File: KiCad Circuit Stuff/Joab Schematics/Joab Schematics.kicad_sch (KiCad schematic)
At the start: 0 parts

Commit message: Added some things
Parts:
- added J1: Conn_02x16_Odd_Even, symbol Connector_Generic:Conn_02x16_Odd_Even
- added U1: TPS613222ADBV, Package_TO_SOT_SMD:SOT-23-5, symbol Regulator_Switching:TPS613222ADBV
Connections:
- new net Battery: J1.14 (Pin_14), U1.1 (SW)
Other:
- note added: "INA219 Battery Chargin mode Charge with USBC 3v3 and 5v regulation (bost to 5, linear down to 3.3)"
- note added: "JOAB YOUR SHIT HERE"
- note added: "PIN Layout 1: Motor2_B_Out 2: Motor2_A_Out 3: Mitir4_A_Out 4: Motor 5: Motor 6: Motor 7: CTRL_Ext_Load2 8: Motor 9: USART2_RX 10: Motor 11: EXT_Load2_Out 12: Usart2_TX 13: Fast_Charge_Ctrl 14: battery 15: rsv 16: i2C1_SCL 17: i2C1_SDA 18: 3v3 out 19: gnd 20: 5v out 21: ext_load1_out 22: HV 23: Gnd 24: motor 25: ctrl ext load1 26: motor 27: motor 28: motor 29: motor 30: motor 31: motor 32: motor"
- company: (none) -> UCT
- title: (none) -> Joab PCP Work
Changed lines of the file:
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@@
 (kicad_sch (version 20230121) (generator eeschema)
   (paper "A4")
-  (label "JOAB YOUR SHIT HERE" (at 132.08 102.87 0) (fields_autoplaced)
+  (title_block
+    (title "Joab PCP Work")
+    (date "2025-03-19")
+    (rev "V0.0")
+    (company "UCT")
+    (comment 4 "KLPJOA002")
+  )
+  (wire (pts (xy 146.05 107.95) (xy 146.05 142.24))
+    (stroke (width 0) (type default))
+  )
+  (wire (pts (xy 146.05 107.95) (xy 168.91 107.95))
+    (stroke (width 0) (type default))
+  )
+  (polyline (pts (xy 68.58 12.7) (xy 68.58 59.69))
+    (stroke (width 0) (type default))
+  )
+  (polyline (pts (xy 12.7 59.69) (xy 68.58 59.69))
+    (stroke (width 0) (type default))
+  )
+  (text "INA219\nBattery Chargin mode\nCharge with USBC\n3v3 and 5v regulation (bost to 5, linear down to 3.3)\n\n"
+    (at 12.7 33.02 0)
     (effects (font (size 1.27 1.27)) (justify left bottom))
   )
+  (text "PIN Layout\n1: Motor2_B_Out\n2: Motor2_A_Out\n3: Mitir4_A_Out\n4: Motor\n5: Motor\n6: Motor\n7: CTRL_Ext_Load2\n8: Motor\n9: USART2_RX\n10: Motor\n11: EXT_Load2_Out\n12: Usart2_TX\n13: Fast_Charge_Ctrl\n14: battery\n15: rsv\n16: i2C1_SCL\n17: i2C1_SDA\n18: 3v3 out\n19: gnd\n20: 5v out\n21: ext_load1_out\n22: HV\n23:	Gnd\n24: motor\n25: ctrl ext load1\n26: motor\n27: motor\n28: motor\n29: motor\n30: motor\n31: motor\n32: motor"
+    (at 76.2 191.77 0)
+    (effects (font (size 1.27 1.27)) (justify left bottom))
+  )
+  (text "JOAB YOUR SHIT HERE" (at 26.67 15.24 0)
+    (effects (font (size 1.27 1.27)) (justify left bottom))
+  )
+  (label "Battery" (at 146.05 137.16 0) (fields_autoplaced)
+    (effects (font (size 1.27 1.27)) (justify left bottom))
+  )
+  (symbol (lib_id "Regulator_Switching:TPS613222ADBV") (at 179.07 110.49 0) (unit 1)
+    (in_bom yes) (on_board yes) (dnp no) (fields_autoplaced)
+    (property "Reference" "U1" (at 179.07 101.6 0)
+      (effects (font (size 1.27 1.27)))
+    )
+    (property "Value" "TPS613222ADBV" (at 179.07 104.14 0)
+      (effects (font (size 1.27 1.27)))
+    )
+    (property "Footprint" "Package_TO_SOT_SMD:SOT-23-5" (at 179.07 130.81 0)
+      (effects (font (size 1.27 1.27)) hide)
+    )
+    (property "Datasheet" "http://www.ti.com/lit/ds/symlink/tps61322.pdf" (at 179.07 114.3 0)
+      (effects (font (size 1.27 1.27)) hide)
+    )
+    (pin "1")
+    (pin "2")
+    (pin "3")
+    (pin "4")
+    (pin "5")
+    (instances
+      (project "Joab Schematics"
+        (path "/40536255-d30b-4646-9a8a-71849f0da59a"
+          (reference "U1") (unit 1)
+        )
+      )
+    )
+  )
+  (symbol (lib_id "Connector_Generic:Conn_02x16_Odd_Even") (at 143.51 149.86 270) (mirror x) (unit 1)
+    (in_bom yes) (on_board yes) (dnp no) (fields_autoplaced)
+    (property "Reference" "J1" (at 120.65 147.955 90)
+      (effects (font (size 1.27 1.27)) (justify right))
+    )
+    (property "Value" "Conn_02x16_Odd_Even" (at 120.65 150.495 90)
+      (effects (font (size 1.27 1.27)) (justify right))
+    )
+    (property "Footprint" "" (at 143.51 149.86 0)
+      (effects (font (size 1.27 1.27)) hide)
+    )
+    (property "Datasheet" "~" (at 143.51 149.86 0)
+      (effects (font (size 1.27 1.27)) hide)
+    )
+    (pin "1")
+    (pin "10")
+    (pin "11")
+    (pin "12")
+    (pin "13")
+    (pin "14")
+    (pin "15")
+    (pin "16")
+    (pin "17")
+    (pin "18")
+    (pin "19")
+    (pin "2")
+    (pin "20")
+    (pin "21")
+    (pin "22")
+    (pin "23")
+    (pin "24")
+    (pin "25")
+    (pin "26")
+    (pin "27")
+    (pin "28")
+    (pin "29")
+    (pin "3")
+    (pin "30")
+    (pin "31")
+    (pin "32")
+    (pin "4")
+    (pin "5")
+    (pin "6")
+    (pin "7")
+    (pin "8")
+    (pin "9")
+    (instances
+      (project "Joab Schematics"
+        (path "/40536255-d30b-4646-9a8a-71849f0da59a"
+          (reference "J1") (unit 1)
+        )
+      )
+    )
+  )
   (sheet_instances

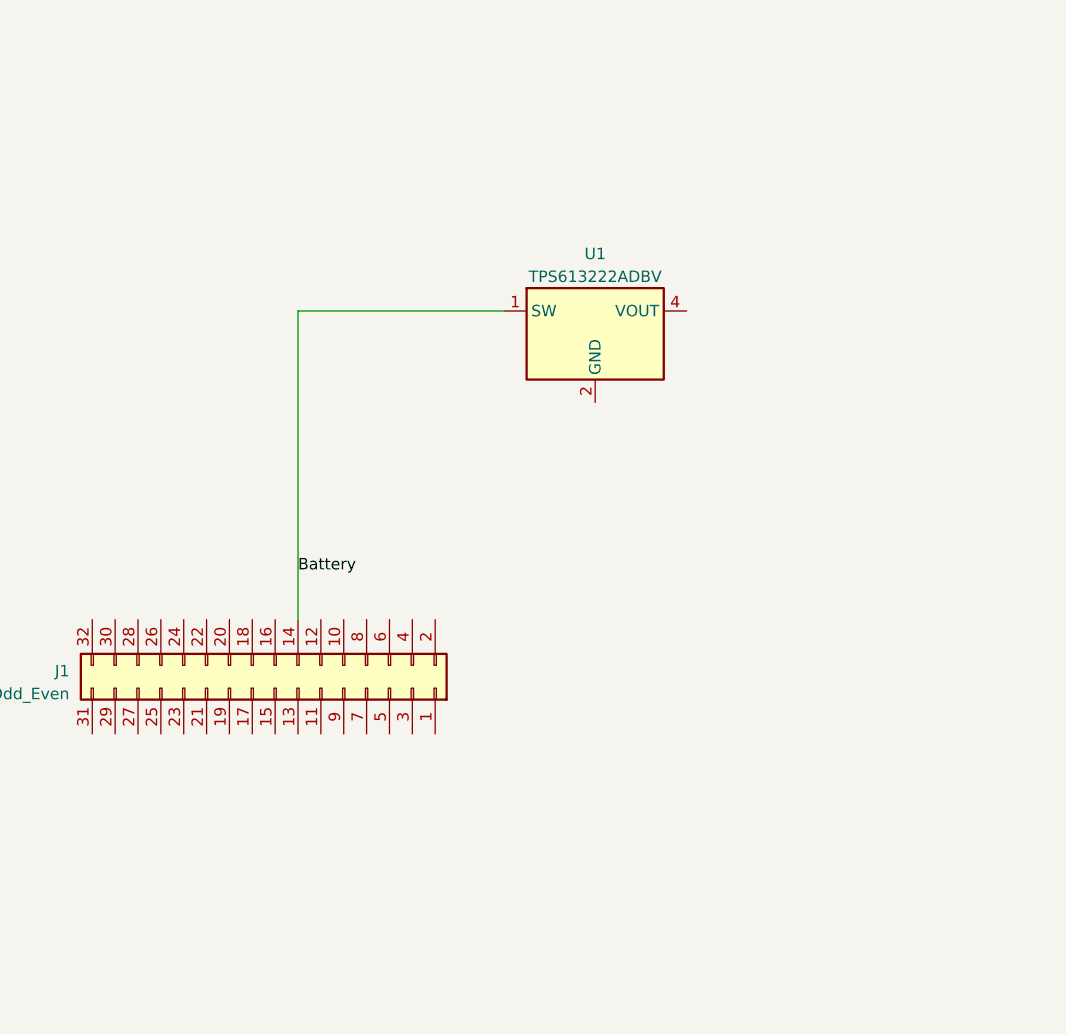
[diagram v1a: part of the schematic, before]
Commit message: Did some voltage Regulation for 5v without calculating values
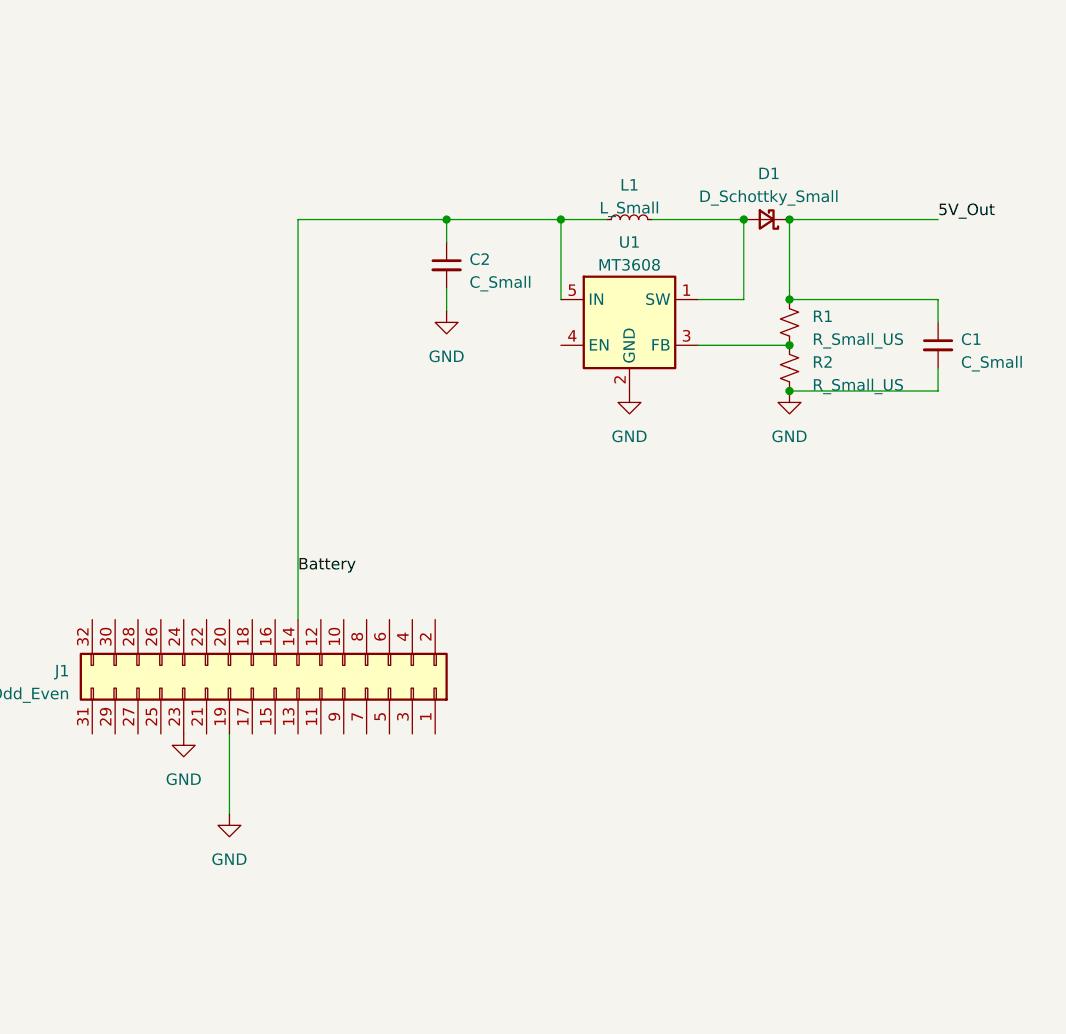
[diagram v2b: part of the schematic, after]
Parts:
- removed U1: TPS613222ADBV, Package_TO_SOT_SMD:SOT-23-5, symbol Regulator_Switching:TPS613222ADBV
- added C1, C2: C_Small, symbol Device:C_Small
- added D1: D_Schottky_Small, symbol Device:D_Schottky_Small
- added L1: L_Small, symbol Device:L_Small
- added R1, R2: R_Small_US, symbol Device:R_Small_US
- added U1: MT3608, Package_TO_SOT_SMD:SOT-23-6, symbol Regulator_Switching:MT3608
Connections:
- net Battery: now also C2.1, L1.1, U1.5 (IN)
- net GND: now reaches J1.19 (Pin_19)
- net GND: now also J1.23 (Pin_23), C1.2, C2.2, R2.2, U1.2 (GND)
- new net: D1.2 (A), L1.2, U1.1 (SW)
- new net: R1.2, R2.1, U1.3 (FB)
- new net 5V_Out: C1.1, D1.1 (K), R1.1

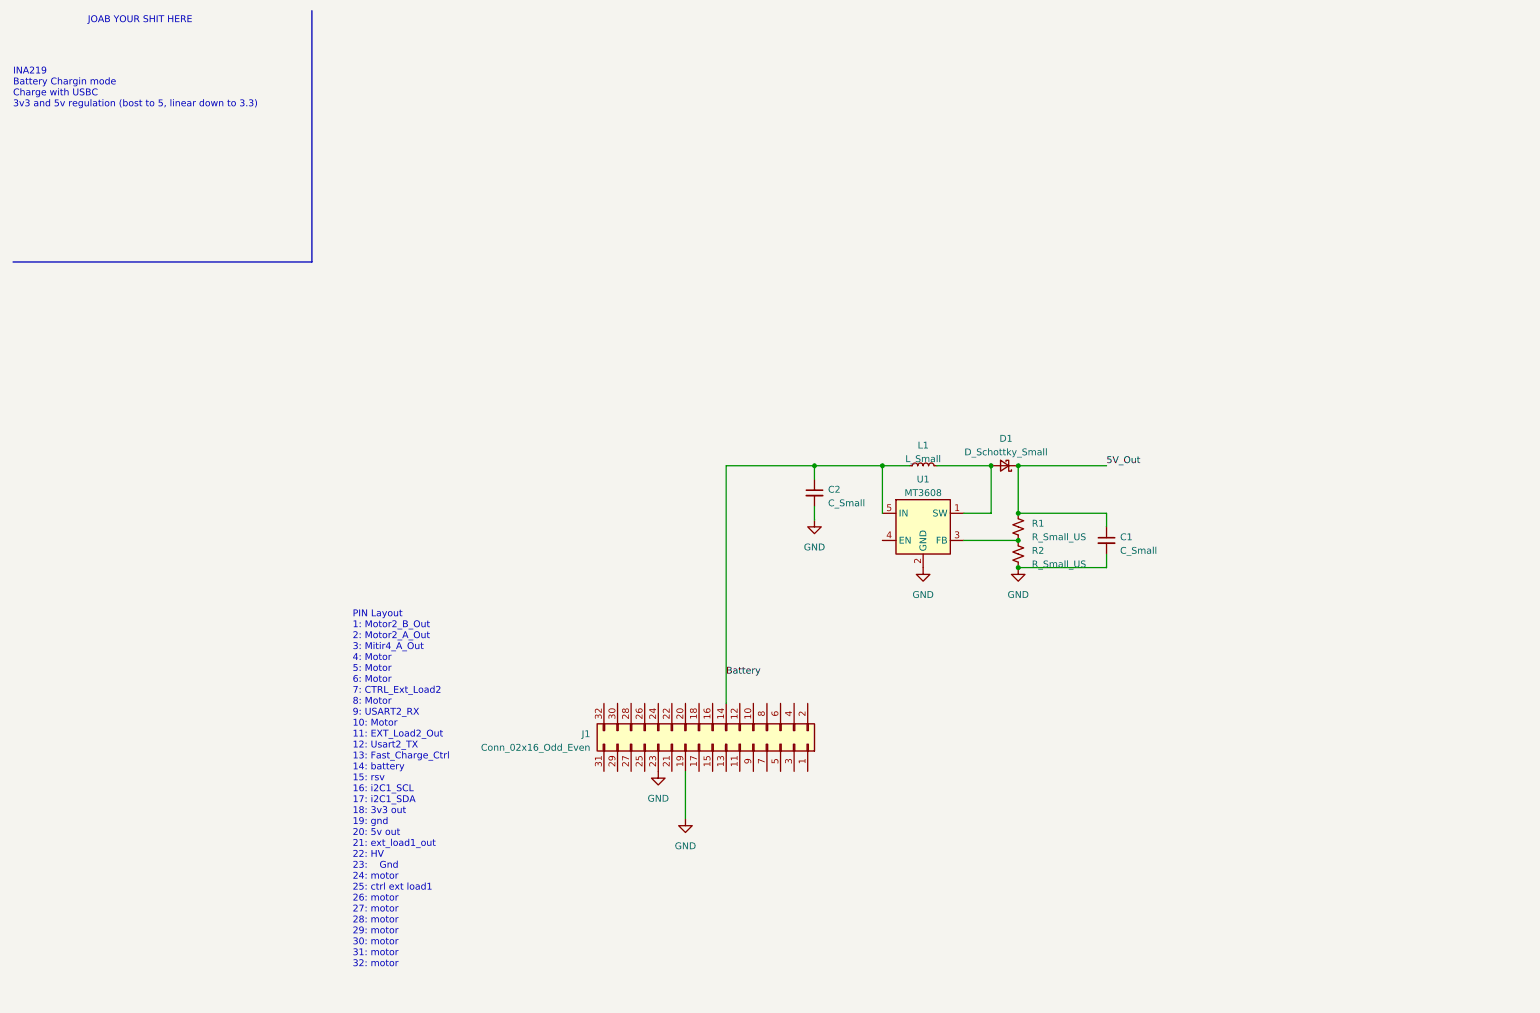
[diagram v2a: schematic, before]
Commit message: Added 5V and 3v3 Regulation, started on battery charging
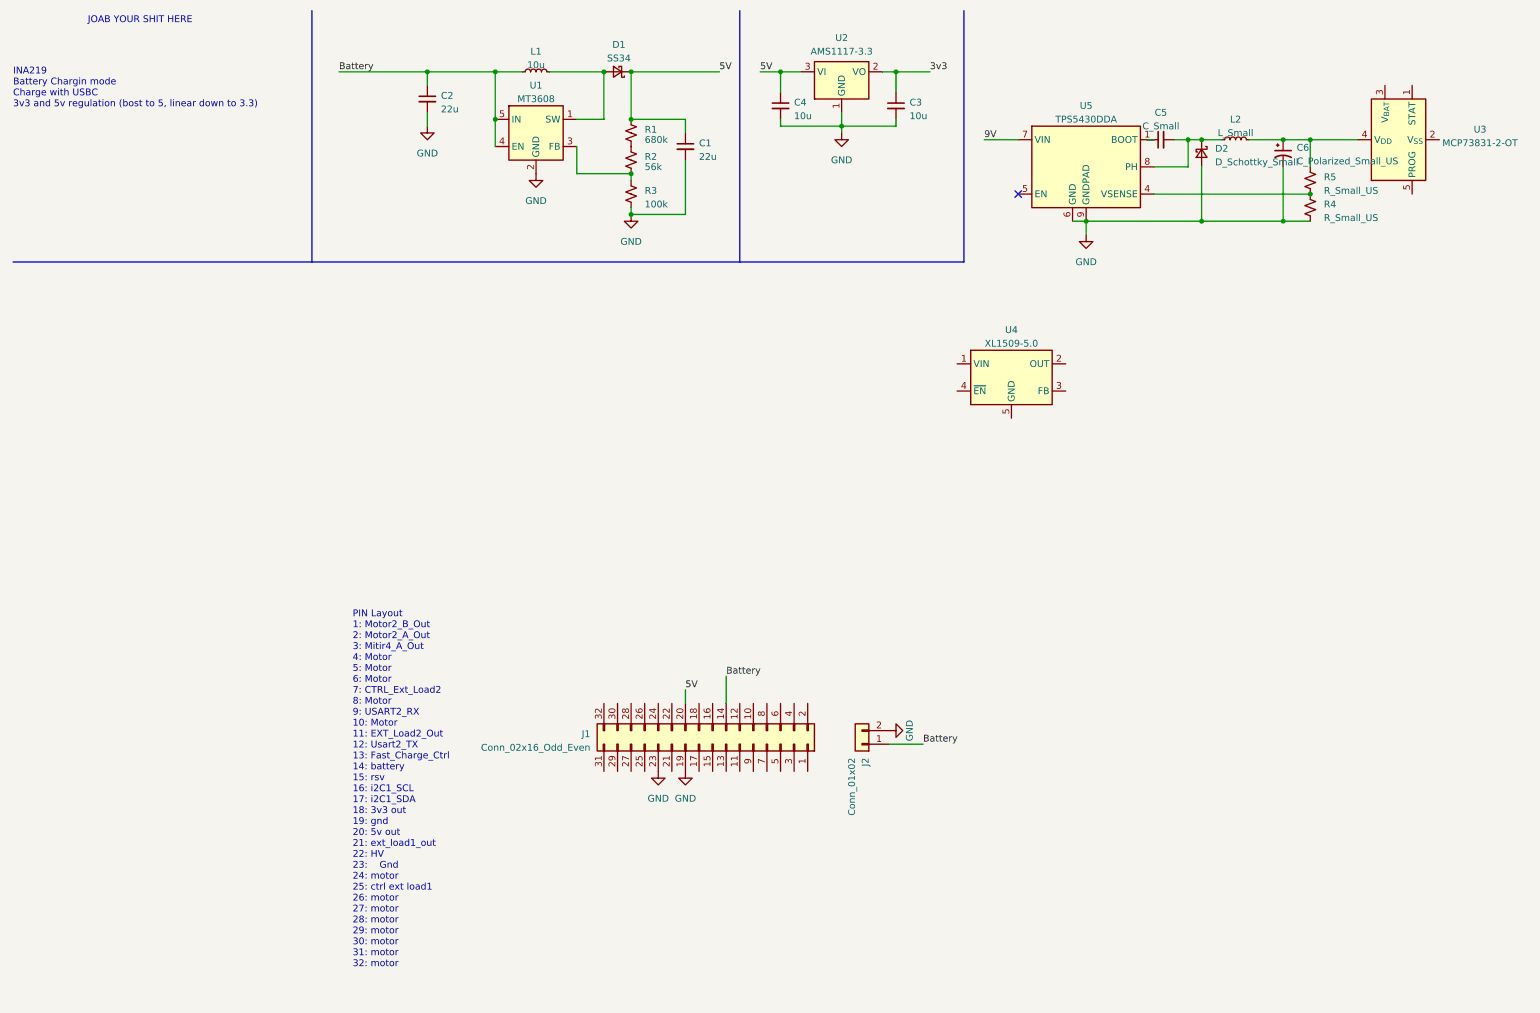
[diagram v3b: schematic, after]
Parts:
- added C3, C4: 10u, symbol Device:C_Small
- added C5: C_Small, symbol Device:C_Small
- added C6: C_Polarized_Small_US, symbol Device:C_Polarized_Small_US
- added D2: D_Schottky_Small, symbol Device:D_Schottky_Small
- added J2: Conn_01x02, symbol Connector_Generic:Conn_01x02
- added L2: L_Small, symbol Device:L_Small
- added R2: 56k, symbol Device:R_Small_US
- added R4, R5: R_Small_US, symbol Device:R_Small_US
- added U2: AMS1117-3.3, Package_TO_SOT_SMD:SOT-223-3_TabPin2, symbol Regulator_Linear:AMS1117-3.3
- added U3: MCP73831-2-OT, Package_TO_SOT_SMD:SOT-23-5, symbol Battery_Management:MCP73831-2-OT
- added U4: XL1509-5.0, Package_SO:SOIC-8_3.9x4.9mm_P1.27mm, symbol Regulator_Switching:XL1509-5.0
- added U5: TPS5430DDA, Package_SO:TI_SO-PowerPAD-8_ThermalVias, symbol Regulator_Switching:TPS5430DDA
- C1, C2: value C_Small -> 22u
- D1: value D_Schottky_Small -> SS34; LCSC (none) -> C8678
- L1: value L_Small -> 10u; LCSC (none) -> C9182
- R1: value R_Small_US -> 680k
- R3: renamed from R2; value R_Small_US -> 100k
- U1: LCSC (none) -> C84817
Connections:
- net 5V_Out is gone; now on net 5V: C1.1, D1.1 (K), R1.1
- net Battery: now also U1.4 (EN), J2.1 (Pin_1)
- net GND: now also C3.2, C4.2, C6.2, D2.2 (A), J2.2 (Pin_2), R4.2, U2.1 (GND), U5.6 (GND), U5.9 (GNDPAD)
- net at R3.1, U1.3 (FB): now also R2.2; no longer R1.2
- net 5V: now reaches J1.20 (Pin_20)
- net 5V: now also C4.1, U2.3 (VI)
- new net: C6.1, L2.2, R5.1, U3.4 (V_{DD})
- new net: U4.5 (GND), U4.6 (GND), U4.7 (GND), U4.8 (GND)
- new net: R1.2, R2.1
- new net: C5.2, D2.1 (K), L2.1, U5.8 (PH)
- new net: C5.1, U5.1 (BOOT)
- new net: R4.1, R5.2, U5.4 (VSENSE)
- new net 3v3: C3.1, U2.2 (VO)
- new net 9V: U5.7 (VIN)
- no-connect marks 0 -> 1
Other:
- moved on the sheet: C1, C2, D1, L1, R1, R3, U1

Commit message: DId battery charger, some labeling and components
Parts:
- removed U4: XL1509-5.0, Package_SO:SOIC-8_3.9x4.9mm_P1.27mm, symbol Regulator_Switching:XL1509-5.0
- added C10, C7, C8, C9: 4.7u, Capacitor_SMD:C_0402_1005Metric_Pad0.74x0.62mm_HandSolder, symbol Device:C_Small
- added Q1: MMBT3904, Package_TO_SOT_SMD:SOT-23, symbol Transistor_BJT:MMBT3904
- added Q2: S8550, Package_TO_SOT_THT:TO-92_Inline, symbol Transistor_BJT:S8550
- added R6: 180k, Resistor_SMD:R_0402_1005Metric_Pad0.72x0.64mm_HandSolder, symbol Device:R_Small_US
- added R7: 1.8k, Resistor_SMD:R_0402_1005Metric_Pad0.72x0.64mm_HandSolder, symbol Device:R_Small_US
- added R8: 5k, Resistor_SMD:R_0402_1005Metric_Pad0.72x0.64mm_HandSolder, symbol Device:R_Small_US
- added R9: 1000k, Resistor_SMD:R_0402_1005Metric_Pad0.72x0.64mm_HandSolder, symbol Device:R_Small_US
- added TP1: L TP 2, TestPoint:TestPoint_2Pads_Pitch2.54mm_Drill0.8mm, symbol Connector:TestPoint
- added TP10, TP3, TP4, TP5, TP6, TP7, TP8, TP9: TestPoint, TestPoint:TestPoint_2Pads_Pitch2.54mm_Drill0.8mm, symbol Connector:TestPoint
- added TP11: 9V TP, TestPoint:TestPoint_2Pads_Pitch2.54mm_Drill0.8mm, symbol Connector:TestPoint
- added TP12: 5V TP, TestPoint:TestPoint_2Pads_Pitch2.54mm_Drill0.8mm, symbol Connector:TestPoint
- added TP13: 3V3 TP, TestPoint:TestPoint_2Pads_Pitch2.54mm_Drill0.8mm, symbol Connector:TestPoint
- added TP14: GND TP, TestPoint:TestPoint_2Pads_Pitch2.54mm_Drill0.8mm, symbol Connector:TestPoint
- added TP15: BAT TP, TestPoint:TestPoint_2Pads_Pitch2.54mm_Drill0.8mm, symbol Connector:TestPoint
- added TP2: L TP 1, TestPoint:TestPoint_2Pads_Pitch2.54mm_Drill0.8mm, symbol Connector:TestPoint
- C1, C2, C3, C4: footprint (none) -> Capacitor_SMD:C_0402_1005Metric_Pad0.74x0.62mm_HandSolder
- C5: value C_Small -> 0.01u; footprint (none) -> Capacitor_SMD:C_0402_1005Metric_Pad0.74x0.62mm_HandSolder
- C6: value C_Polarized_Small_US -> 220u; footprint (none) -> Capacitor_SMD:C_0402_1005Metric_Pad0.74x0.62mm_HandSolder
- D1: footprint (none) -> Diode_SMD:D_SMA_Handsoldering
- D2: value D_Schottky_Small -> SS34; footprint (none) -> Diode_SMD:D_SMA_Handsoldering; LCSC (none) -> C8678
- L1: footprint (none) -> Inductor_SMD:L_0402_1005Metric_Pad0.77x0.64mm_HandSolder
- L2: footprint (none) -> Inductor_SMD:L_0402_1005Metric_Pad0.77x0.64mm_HandSolder; LCSC (none) -> C475913
- R1, R2, R3: footprint (none) -> Resistor_SMD:R_0402_1005Metric_Pad0.72x0.64mm_HandSolder
- R4: value R_Small_US -> 3.3k; footprint (none) -> Resistor_SMD:R_0402_1005Metric_Pad0.72x0.64mm_HandSolder
- R5: value R_Small_US -> 10k; footprint (none) -> Resistor_SMD:R_0402_1005Metric_Pad0.72x0.64mm_HandSolder
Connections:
- net 3v3 is gone; now on net +3V3: C3.1, U2.2 (VO)
- net 9V is gone; now on net +9V: U5.7 (VIN)
- net Battery: now also U3.3 (V_{BAT}), C10.2, TP15.1, TP2.1, TP9.1
- net GND: now also U3.2 (V_{SS}), C10.1, C7.1, C8.1, C9.1, Q1.2 (E), R6.2, R8.2, TP10.1, TP14.1, TP5.1, TP8.1
- net Battey_Charger_VDD: now reaches C6.1, L2.2, R5.1, U3.4 (V_{DD})
- net Battey_Charger_VDD: now also C9.2
- net at U3.5 (PROG): now also Q2.3 (C), R7.1
- net at D1.2 (A), L1.2, U1.1 (SW): now also TP1.1
- net at R2.2, R3.1, U1.3 (FB): now also TP7.1
- net at R4.1, R5.2, U5.4 (VSENSE): now also R6.1
- net Fast_Charge_CTRL: now reaches J1.13 (Pin_13)
- net Fast_Charge_CTRL: now also R9.1
- net +3V3: now reaches J1.18 (Pin_18)
- net +3V3: now also TP13.1
- net +9V: now reaches J1.22 (Pin_22)
- net +9V: now also C7.2, C8.2, TP11.1
- net 5V renamed +5V
- net +5V: now also TP12.1, TP3.1, TP4.1, TP6.1
- new net: Q2.1 (E), R8.1
- new net: Q1.1 (B), Q1.3 (C), Q2.2 (B), R7.2, R9.2
- no-connect marks 1 -> 2
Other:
- note added: "3V3 linear regulator to get 3V3 from 5V"
- note added: "5V Boost converter to obtain 5V from battery"
- note added: "Float enable to set default turn on"
- note added: "Global Test Points"
- moved on the sheet: C5, C6, D2, L2, R4, R5, U3, U5
